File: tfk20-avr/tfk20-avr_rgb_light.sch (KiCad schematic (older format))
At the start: 12 parts

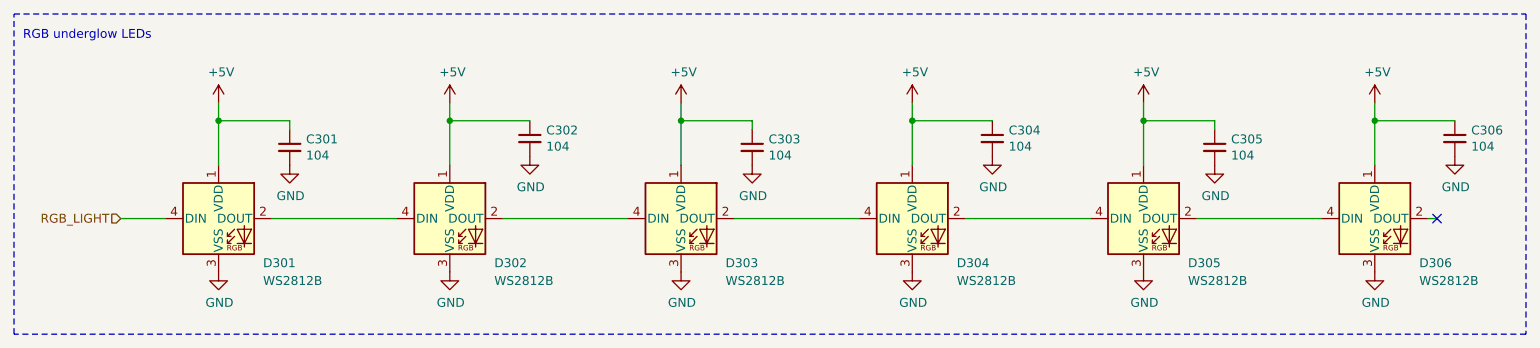
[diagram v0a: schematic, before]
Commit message: Add ISP header
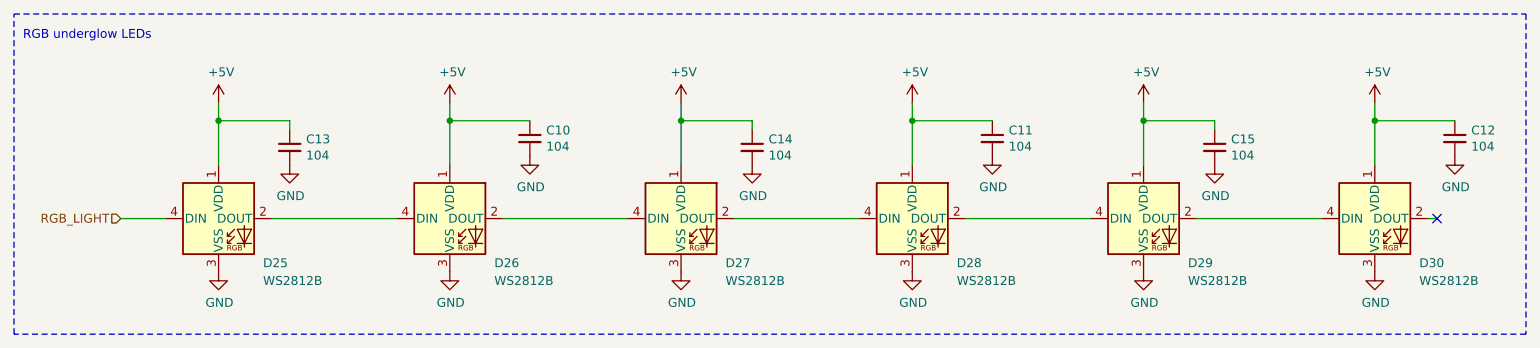
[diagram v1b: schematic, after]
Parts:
- renumbered C302 to C10, C304 to C11, C306 to C12, C301 to C13, C303 to C14, C305 to C15, D301 to D25, D302 to D26, D303 to D27, D304 to D28, D305 to D29, D306 to D30

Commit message: Assign some footprints
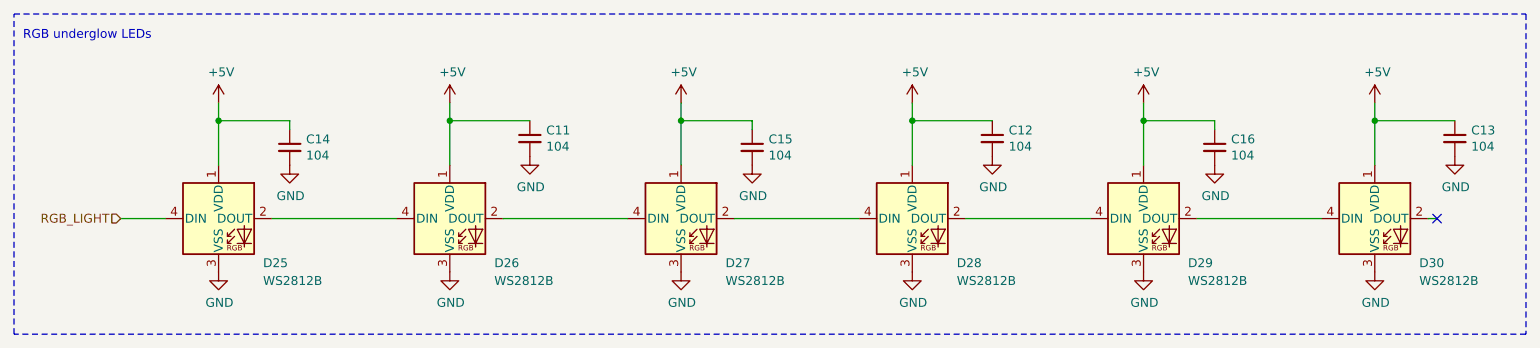
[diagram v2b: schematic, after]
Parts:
- C11: renamed from C10; footprint (none) -> Capacitor_SMD:C_0805_2012Metric_Pad1.18x1.45mm_HandSolder
- C12: renamed from C11; footprint (none) -> Capacitor_SMD:C_0805_2012Metric_Pad1.18x1.45mm_HandSolder
- C13: renamed from C12; footprint (none) -> Capacitor_SMD:C_0805_2012Metric_Pad1.18x1.45mm_HandSolder
- C14: renamed from C13; footprint (none) -> Capacitor_SMD:C_0805_2012Metric_Pad1.18x1.45mm_HandSolder
- C15: renamed from C14; footprint (none) -> Capacitor_SMD:C_0805_2012Metric_Pad1.18x1.45mm_HandSolder
- C16: renamed from C15; footprint (none) -> Capacitor_SMD:C_0805_2012Metric_Pad1.18x1.45mm_HandSolder
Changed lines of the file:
@@
 P 3050 3750
 AR Path="/602C3063/601B5D07" Ref="C?"  Part="1"
-AR Path="/602C340B/601B5D07" Ref="C13"  Part="1"
-F 0 "C13" H 3142 3796 50  0000 L CNN
+AR Path="/602C340B/601B5D07" Ref="C14"  Part="1"
+F 0 "C14" H 3142 3796 50  0000 L CNN
 F 1 "104" H 3142 3705 50  0000 L CNN
-F 2 "" H 3050 3750 50  0001 C CNN
+F 2 "Capacitor_SMD:C_0805_2012Metric_Pad1.18x1.45mm_HandSolder" H 3050 3750 50  0001 C CNN
 F 3 "~" H 3050 3750 50  0001 C CNN
 	1    3050 3750
@@
 P 4400 3700
 AR Path="/602C3063/601B5D2A" Ref="C?"  Part="1"
-AR Path="/602C340B/601B5D2A" Ref="C10"  Part="1"
-F 0 "C10" H 4492 3746 50  0000 L CNN
+AR Path="/602C340B/601B5D2A" Ref="C11"  Part="1"
+F 0 "C11" H 4492 3746 50  0000 L CNN
 F 1 "104" H 4492 3655 50  0000 L CNN
-F 2 "" H 4400 3700 50  0001 C CNN
+F 2 "Capacitor_SMD:C_0805_2012Metric_Pad1.18x1.45mm_HandSolder" H 4400 3700 50  0001 C CNN
 F 3 "~" H 4400 3700 50  0001 C CNN
 	1    4400 3700
@@
 P 5650 3750
 AR Path="/602C3063/601B5D4C" Ref="C?"  Part="1"
-AR Path="/602C340B/601B5D4C" Ref="C14"  Part="1"
-F 0 "C14" H 5742 3796 50  0000 L CNN
+AR Path="/602C340B/601B5D4C" Ref="C15"  Part="1"
+F 0 "C15" H 5742 3796 50  0000 L CNN
 F 1 "104" H 5742 3705 50  0000 L CNN
-F 2 "" H 5650 3750 50  0001 C CNN
+F 2 "Capacitor_SMD:C_0805_2012Metric_Pad1.18x1.45mm_HandSolder" H 5650 3750 50  0001 C CNN
 F 3 "~" H 5650 3750 50  0001 C CNN
 	1    5650 3750
@@
 P 7000 3700
 AR Path="/602C3063/601B5D6F" Ref="C?"  Part="1"
-AR Path="/602C340B/601B5D6F" Ref="C11"  Part="1"
-F 0 "C11" H 7092 3746 50  0000 L CNN
+AR Path="/602C340B/601B5D6F" Ref="C12"  Part="1"
+F 0 "C12" H 7092 3746 50  0000 L CNN
 F 1 "104" H 7092 3655 50  0000 L CNN
-F 2 "" H 7000 3700 50  0001 C CNN
+F 2 "Capacitor_SMD:C_0805_2012Metric_Pad1.18x1.45mm_HandSolder" H 7000 3700 50  0001 C CNN
 F 3 "~" H 7000 3700 50  0001 C CNN
 	1    7000 3700
@@
 P 8250 3750
 AR Path="/602C3063/60DF2224" Ref="C?"  Part="1"
-AR Path="/602C340B/60DF2224" Ref="C15"  Part="1"
-F 0 "C15" H 8342 3796 50  0000 L CNN
+AR Path="/602C340B/60DF2224" Ref="C16"  Part="1"
+F 0 "C16" H 8342 3796 50  0000 L CNN
 F 1 "104" H 8342 3705 50  0000 L CNN
-F 2 "" H 8250 3750 50  0001 C CNN
+F 2 "Capacitor_SMD:C_0805_2012Metric_Pad1.18x1.45mm_HandSolder" H 8250 3750 50  0001 C CNN
 F 3 "~" H 8250 3750 50  0001 C CNN
 	1    8250 3750
@@
 P 9600 3700
 AR Path="/602C3063/60DF2247" Ref="C?"  Part="1"
-AR Path="/602C340B/60DF2247" Ref="C12"  Part="1"
-F 0 "C12" H 9692 3746 50  0000 L CNN
+AR Path="/602C340B/60DF2247" Ref="C13"  Part="1"
+F 0 "C13" H 9692 3746 50  0000 L CNN
 F 1 "104" H 9692 3655 50  0000 L CNN
-F 2 "" H 9600 3700 50  0001 C CNN
+F 2 "Capacitor_SMD:C_0805_2012Metric_Pad1.18x1.45mm_HandSolder" H 9600 3700 50  0001 C CNN
 F 3 "~" H 9600 3700 50  0001 C CNN
 	1    9600 3700

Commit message: Place all footprints on PCB
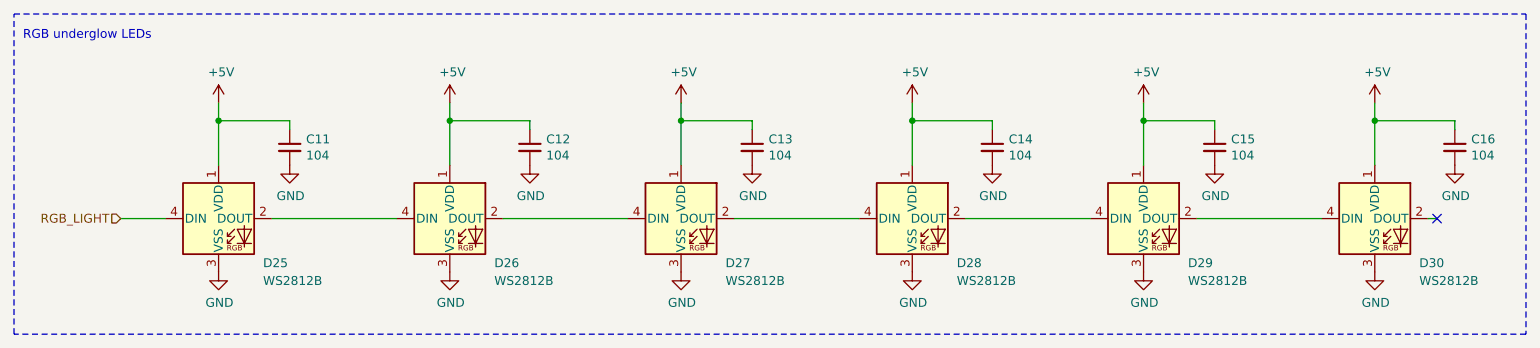
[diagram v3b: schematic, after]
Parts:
- renumbered C14 to C11, C11 to C12, C15 to C13, C12 to C14, C16 to C15, C13 to C16
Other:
- moved on the sheet: C12, C14, C16
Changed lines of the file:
@@
 P 3050 3750
 AR Path="/602C3063/601B5D07" Ref="C?"  Part="1"
-AR Path="/602C340B/601B5D07" Ref="C14"  Part="1"
-F 0 "C14" H 3142 3796 50  0000 L CNN
+AR Path="/602C340B/601B5D07" Ref="C11"  Part="1"
+F 0 "C11" H 3142 3796 50  0000 L CNN
 F 1 "104" H 3142 3705 50  0000 L CNN
 F 2 "Capacitor_SMD:C_0805_2012Metric_Pad1.18x1.45mm_HandSolder" H 3050 3750 50  0001 C CNN
@@
 P 3050 3850
 AR Path="/602C3063/601B5D10" Ref="#PWR?"  Part="1"
-AR Path="/602C340B/601B5D10" Ref="#PWR030"  Part="1"
-F 0 "#PWR030" H 3050 3600 50  0001 C CNN
+AR Path="/602C340B/601B5D10" Ref="#PWR027"  Part="1"
+F 0 "#PWR027" H 3050 3600 50  0001 C CNN
 F 1 "GND" H 3055 3677 50  0000 C CNN
 F 2 "" H 3050 3850 50  0001 C CNN
@@
 L Device:C_Small C?
 U 1 1 601B5D2A
-P 4400 3700
+P 4400 3750
 AR Path="/602C3063/601B5D2A" Ref="C?"  Part="1"
-AR Path="/602C340B/601B5D2A" Ref="C11"  Part="1"
-F 0 "C11" H 4492 3746 50  0000 L CNN
-F 1 "104" H 4492 3655 50  0000 L CNN
-F 2 "Capacitor_SMD:C_0805_2012Metric_Pad1.18x1.45mm_HandSolder" H 4400 3700 50  0001 C CNN
-F 3 "~" H 4400 3700 50  0001 C CNN
-	1    4400 3700
+AR Path="/602C340B/601B5D2A" Ref="C12"  Part="1"
+F 0 "C12" H 4492 3796 50  0000 L CNN
+F 1 "104" H 4492 3705 50  0000 L CNN
+F 2 "Capacitor_SMD:C_0805_2012Metric_Pad1.18x1.45mm_HandSolder" H 4400 3750 50  0001 C CNN
+F 3 "~" H 4400 3750 50  0001 C CNN
+	1    4400 3750
 	1    0    0    -1
 $EndComp
@@
 L power:GND #PWR?
 U 1 1 601B5D32
-P 4400 3800
+P 4400 3850
 AR Path="/602C3063/601B5D32" Ref="#PWR?"  Part="1"
-AR Path="/602C340B/601B5D32" Ref="#PWR027"  Part="1"
-F 0 "#PWR027" H 4400 3550 50  0001 C CNN
-F 1 "GND" H 4405 3627 50  0000 C CNN
-F 2 "" H 4400 3800 50  0001 C CNN
-F 3 "" H 4400 3800 50  0001 C CNN
-	1    4400 3800
+AR Path="/602C340B/601B5D32" Ref="#PWR028"  Part="1"
+F 0 "#PWR028" H 4400 3600 50  0001 C CNN
+F 1 "GND" H 4405 3677 50  0000 C CNN
+F 2 "" H 4400 3850 50  0001 C CNN
+F 3 "" H 4400 3850 50  0001 C CNN
+	1    4400 3850
 	1    0    0    -1
 $EndComp
@@
 P 5650 3750
 AR Path="/602C3063/601B5D4C" Ref="C?"  Part="1"
-AR Path="/602C340B/601B5D4C" Ref="C15"  Part="1"
-F 0 "C15" H 5742 3796 50  0000 L CNN
+AR Path="/602C340B/601B5D4C" Ref="C13"  Part="1"
+F 0 "C13" H 5742 3796 50  0000 L CNN
 F 1 "104" H 5742 3705 50  0000 L CNN
 F 2 "Capacitor_SMD:C_0805_2012Metric_Pad1.18x1.45mm_HandSolder" H 5650 3750 50  0001 C CNN
@@
 P 5650 3850
 AR Path="/602C3063/601B5D55" Ref="#PWR?"  Part="1"
-AR Path="/602C340B/601B5D55" Ref="#PWR031"  Part="1"
-F 0 "#PWR031" H 5650 3600 50  0001 C CNN
+AR Path="/602C340B/601B5D55" Ref="#PWR029"  Part="1"
+F 0 "#PWR029" H 5650 3600 50  0001 C CNN
 F 1 "GND" H 5655 3677 50  0000 C CNN
 F 2 "" H 5650 3850 50  0001 C CNN
@@
 L Device:C_Small C?
 U 1 1 601B5D6F
-P 7000 3700
+P 7000 3750
 AR Path="/602C3063/601B5D6F" Ref="C?"  Part="1"
-AR Path="/602C340B/601B5D6F" Ref="C12"  Part="1"
-F 0 "C12" H 7092 3746 50  0000 L CNN
-F 1 "104" H 7092 3655 50  0000 L CNN
-F 2 "Capacitor_SMD:C_0805_2012Metric_Pad1.18x1.45mm_HandSolder" H 7000 3700 50  0001 C CNN
-F 3 "~" H 7000 3700 50  0001 C CNN
-	1    7000 3700
+AR Path="/602C340B/601B5D6F" Ref="C14"  Part="1"
+F 0 "C14" H 7092 3796 50  0000 L CNN
+F 1 "104" H 7092 3705 50  0000 L CNN
+F 2 "Capacitor_SMD:C_0805_2012Metric_Pad1.18x1.45mm_HandSolder" H 7000 3750 50  0001 C CNN
+F 3 "~" H 7000 3750 50  0001 C CNN
+	1    7000 3750
 	1    0    0    -1
 $EndComp
@@
 L power:GND #PWR?
 U 1 1 601B5D77
-P 7000 3800
+P 7000 3850
 AR Path="/602C3063/601B5D77" Ref="#PWR?"  Part="1"
-AR Path="/602C340B/601B5D77" Ref="#PWR028"  Part="1"
-F 0 "#PWR028" H 7000 3550 50  0001 C CNN
-F 1 "GND" H 7005 3627 50  0000 C CNN
-F 2 "" H 7000 3800 50  0001 C CNN
-F 3 "" H 7000 3800 50  0001 C CNN
-	1    7000 3800
+AR Path="/602C340B/601B5D77" Ref="#PWR030"  Part="1"
+F 0 "#PWR030" H 7000 3600 50  0001 C CNN
+F 1 "GND" H 7005 3677 50  0000 C CNN
+F 2 "" H 7000 3850 50  0001 C CNN
+F 3 "" H 7000 3850 50  0001 C CNN
+	1    7000 3850
 	1    0    0    -1
 $EndComp
@@
 P 8250 3750
 AR Path="/602C3063/60DF2224" Ref="C?"  Part="1"
-AR Path="/602C340B/60DF2224" Ref="C16"  Part="1"
-F 0 "C16" H 8342 3796 50  0000 L CNN
+AR Path="/602C340B/60DF2224" Ref="C15"  Part="1"
+F 0 "C15" H 8342 3796 50  0000 L CNN
 F 1 "104" H 8342 3705 50  0000 L CNN
 F 2 "Capacitor_SMD:C_0805_2012Metric_Pad1.18x1.45mm_HandSolder" H 8250 3750 50  0001 C CNN
@@
 P 8250 3850
 AR Path="/602C3063/60DF222D" Ref="#PWR?"  Part="1"
-AR Path="/602C340B/60DF222D" Ref="#PWR032"  Part="1"
-F 0 "#PWR032" H 8250 3600 50  0001 C CNN
+AR Path="/602C340B/60DF222D" Ref="#PWR031"  Part="1"
+F 0 "#PWR031" H 8250 3600 50  0001 C CNN
 F 1 "GND" H 8255 3677 50  0000 C CNN
 F 2 "" H 8250 3850 50  0001 C CNN
@@
 L Device:C_Small C?
 U 1 1 60DF2247
-P 9600 3700
+P 9600 3750
 AR Path="/602C3063/60DF2247" Ref="C?"  Part="1"
-AR Path="/602C340B/60DF2247" Ref="C13"  Part="1"
-F 0 "C13" H 9692 3746 50  0000 L CNN
-F 1 "104" H 9692 3655 50  0000 L CNN
-F 2 "Capacitor_SMD:C_0805_2012Metric_Pad1.18x1.45mm_HandSolder" H 9600 3700 50  0001 C CNN
-F 3 "~" H 9600 3700 50  0001 C CNN
-	1    9600 3700
+AR Path="/602C340B/60DF2247" Ref="C16"  Part="1"
+F 0 "C16" H 9692 3796 50  0000 L CNN
+F 1 "104" H 9692 3705 50  0000 L CNN
+F 2 "Capacitor_SMD:C_0805_2012Metric_Pad1.18x1.45mm_HandSolder" H 9600 3750 50  0001 C CNN
+F 3 "~" H 9600 3750 50  0001 C CNN
+	1    9600 3750
 	1    0    0    -1
 $EndComp
@@
 L power:GND #PWR?
 U 1 1 60DF224F
-P 9600 3800
+P 9600 3850
 AR Path="/602C3063/60DF224F" Ref="#PWR?"  Part="1"
-AR Path="/602C340B/60DF224F" Ref="#PWR029"  Part="1"
-F 0 "#PWR029" H 9600 3550 50  0001 C CNN
-F 1 "GND" H 9605 3627 50  0000 C CNN
-F 2 "" H 9600 3800 50  0001 C CNN
-F 3 "" H 9600 3800 50  0001 C CNN
-	1    9600 3800
+AR Path="/602C340B/60DF224F" Ref="#PWR032"  Part="1"
+F 0 "#PWR032" H 9600 3600 50  0001 C CNN
+F 1 "GND" H 9605 3677 50  0000 C CNN
+F 2 "" H 9600 3850 50  0001 C CNN
+F 3 "" H 9600 3850 50  0001 C CNN
+	1    9600 3850
 	1    0    0    -1
 $EndComp
@@
 Wire Notes Line
 	10000 4800 1500 4800
+Wire Wire Line
+	4400 3600 4400 3650
+Wire Wire Line
+	7000 3600 7000 3650
+Wire Wire Line
+	9600 3600 9600 3650
 $EndSCHEMATC
